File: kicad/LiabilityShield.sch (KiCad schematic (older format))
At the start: 8 parts, among them P1 Power, P2 Analog, P3 Digital, P4 Digital, P5 CONN_01X01, P6 CONN_01X01, P7 CONN_01X01, P8 CONN_01X01

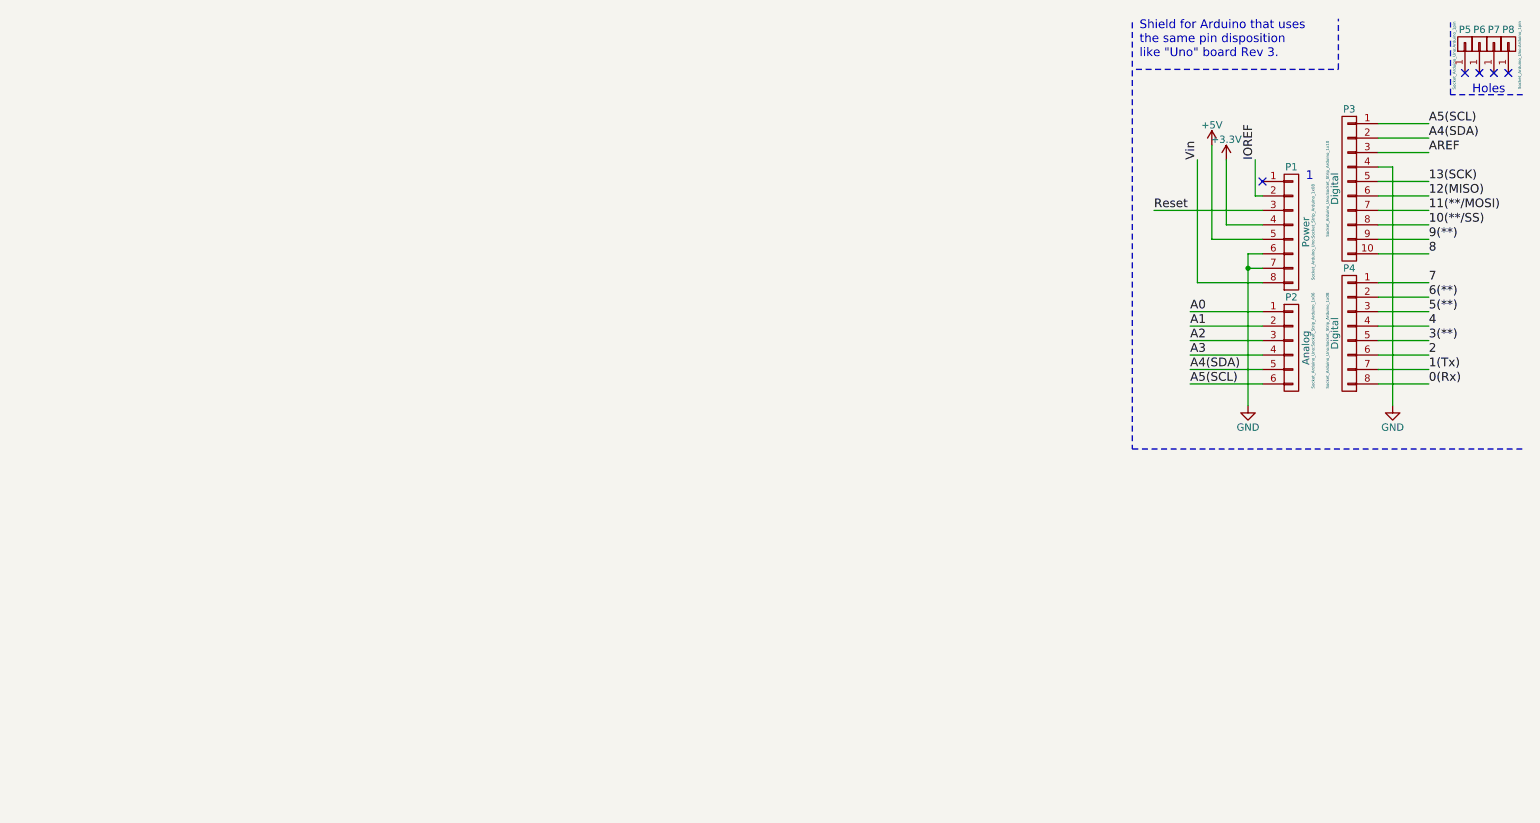
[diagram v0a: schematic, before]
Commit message: Board defined
Minimal schematic and board layout
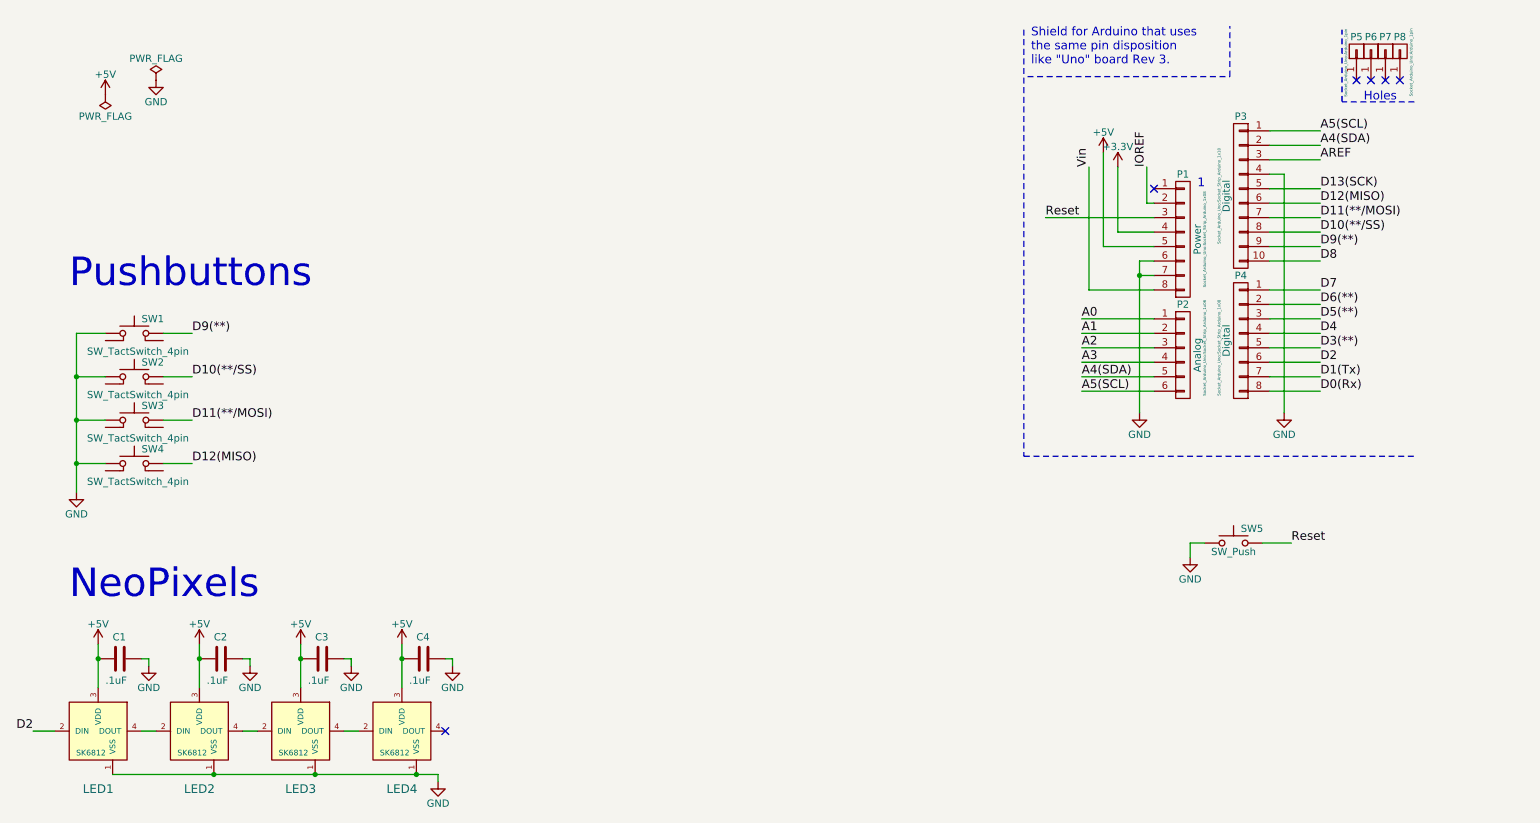
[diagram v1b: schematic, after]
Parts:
- added C1, C2, C3, C4: .1uF, Capacitors_SMD:C_0805_HandSoldering, symbol C
- added LED1, LED2, LED3, LED4: SK6812, lib_fp:LED_5050_4pin, symbol SK6812
- added SW1, SW2, SW3, SW4: SW_TactSwitch_4pin, lib_fp:TactSwitch_12.5_5, symbol SW_TactSwitch_4pin
- added SW5: SW_Push, lib_fp:TactSwitch_6.5_4.5, symbol SW_Push
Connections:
- net +5V: now also C1.2, C2.2, C3.2, C4.2, LED1.3 (VDD), LED2.3 (VDD), LED3.3 (VDD), LED4.3 (VDD)
- net GND: now also C1.1, C2.1, C3.1, C4.1, LED1.1 (VSS), LED2.1 (VSS), LED3.1 (VSS), LED4.1 (VSS), SW1.1 (A), SW2.1 (A), SW3.1 (A), SW4.1 (A), SW5.1
- net Reset: now also SW5.2
- net 0(Rx) renamed D0(Rx)
- net 1(Tx) renamed D1(Tx)
- net 10(**/SS) renamed D10(**/SS)
- net D10(**/SS): now also SW2.3 (B)
- net 11(**/MOSI) renamed D11(**/MOSI)
- net D11(**/MOSI): now also SW3.3 (B)
- net 12(MISO) renamed D12(MISO)
- net D12(MISO): now also SW4.3 (B)
- net 13(SCK) renamed D13(SCK)
- net 2 renamed D2
- net D2: now also LED1.2 (DIN)
- net 3(**) renamed D3(**)
- net 4 renamed D4
- net 5(**) renamed D5(**)
- net 6(**) renamed D6(**)
- net 7 renamed D7
- net 8 renamed D8
- net 9(**) renamed D9(**)
- net D9(**): now also SW1.3 (B)
- new net: LED1.4 (DOUT), LED2.2 (DIN)
- new net: LED2.4 (DOUT), LED3.2 (DIN)
- new net: LED3.4 (DOUT), LED4.2 (DIN)
- no-connect marks 5 -> 6
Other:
- note added: "NeoPixels"
- note added: "Pushbuttons"
- moved on the sheet: P1, P2, P3, P4, P5, P6, P7, P8
